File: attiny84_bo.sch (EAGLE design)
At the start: 9 parts, among them J1 AVR_SPI_PRG_6NS, Y1 16MHz

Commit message: initial placement
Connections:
- new net N$6: JP1.10, U$1.(PCINT10/INT0/OC0A/CKOUT)PB2
- net +5V: now also JP1.2, LED1.A
- net GND: now also JP1.16, JP1.4, JP1.6, JP1.8
- net N$1: now also LED1.C
- net PB0/XTAL1: now also JP1.14
- net PB1/XTAL2: now also JP1.12
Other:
- moved on the sheet: LED1
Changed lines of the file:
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@@
 <part name="P+1" library="supply1" deviceset="+5V" device=""/>
 <part name="JP1" library="pinhead" deviceset="PINHD-2X8" device=""/>
+<part name="GND1" library="supply1" deviceset="GND" device=""/>
+<part name="P+2" library="supply1" deviceset="+5V" device=""/>
+<part name="GND2" library="supply1" deviceset="GND" device=""/>
 </parts>
 <sheets>
@@
 <instance part="P+5" gate="1" x="76.2" y="111.76"/>
 <instance part="C1" gate="G$1" x="38.1" y="96.52" rot="R90"/>
-<instance part="LED1" gate="G$1" x="55.88" y="124.46" rot="R270"/>
+<instance part="LED1" gate="G$1" x="109.22" y="91.44" rot="R270"/>
 <instance part="C2" gate="G$1" x="38.1" y="106.68" rot="R90"/>
 <instance part="CX0" gate="G$1" x="20.32" y="104.14" rot="R90"/>
@@
 <instance part="P+1" gate="1" x="20.32" y="86.36"/>
 <instance part="JP1" gate="A" x="121.92" y="63.5"/>
+<instance part="GND1" gate="1" x="127" y="50.8"/>
+<instance part="P+2" gate="1" x="127" y="73.66"/>
+<instance part="GND2" gate="1" x="129.54" y="68.58" rot="R90"/>
 </instances>
 <busses>
@@
 <pinref part="GND3" gate="1" pin="GND"/>
 </segment>
+<segment>
+<pinref part="JP1" gate="A" pin="16"/>
+<pinref part="GND1" gate="1" pin="GND"/>
+</segment>
+<segment>
+<pinref part="JP1" gate="A" pin="4"/>
+<pinref part="GND2" gate="1" pin="GND"/>
+<pinref part="JP1" gate="A" pin="8"/>
+<wire x1="127" y1="68.58" x2="127" y2="66.04" width="0.1524" layer="91"/>
+<junction x="127" y="68.58"/>
+<pinref part="JP1" gate="A" pin="6"/>
+<junction x="127" y="66.04"/>
+<wire x1="127" y1="66.04" x2="127" y2="63.5" width="0.1524" layer="91"/>
+<junction x="127" y="63.5"/>
+</segment>
 </net>
 <net name="+5V" class="1">
@@
 <wire x1="78.74" y1="119.38" x2="35.56" y2="119.38" width="0.1524" layer="91"/>
 <wire x1="35.56" y1="119.38" x2="35.56" y2="106.68" width="0.1524" layer="91"/>
+<pinref part="LED1" gate="G$1" pin="A"/>
+<wire x1="78.74" y1="109.22" x2="111.76" y2="109.22" width="0.1524" layer="91"/>
+<wire x1="111.76" y1="109.22" x2="111.76" y2="91.44" width="0.1524" layer="91"/>
 </segment>
 <segment>
 <pinref part="U$1" gate="G$1" pin="VCC"/>
 <pinref part="P+1" gate="1" pin="+5V"/>
+</segment>
+<segment>
+<pinref part="JP1" gate="A" pin="2"/>
+<pinref part="P+2" gate="1" pin="+5V"/>
 </segment>
 </net>
@@
 <wire x1="10.16" y1="43.18" x2="10.16" y2="91.44" width="0.1524" layer="91"/>
 <wire x1="25.4" y1="91.44" x2="10.16" y2="91.44" width="0.1524" layer="91"/>
+<wire x1="78.74" y1="76.2" x2="137.16" y2="76.2" width="0.1524" layer="91"/>
+<wire x1="137.16" y1="76.2" x2="137.16" y2="55.88" width="0.1524" layer="91"/>
+<pinref part="JP1" gate="A" pin="14"/>
+<wire x1="137.16" y1="55.88" x2="127" y2="55.88" width="0.1524" layer="91"/>
+<junction x="78.74" y="76.2"/>
 </segment>
 </net>
@@
 <wire x1="76.2" y1="78.74" x2="71.12" y2="78.74" width="0.1524" layer="91"/>
 <junction x="25.4" y="104.14"/>
+<wire x1="76.2" y1="78.74" x2="139.7" y2="78.74" width="0.1524" layer="91"/>
+<wire x1="139.7" y1="78.74" x2="139.7" y2="58.42" width="0.1524" layer="91"/>
+<pinref part="JP1" gate="A" pin="12"/>
+<wire x1="127" y1="58.42" x2="139.7" y2="58.42" width="0.1524" layer="91"/>
 </segment>
 </net>
@@
 <pinref part="JP1" gate="A" pin="15"/>
 <wire x1="96.52" y1="53.34" x2="119.38" y2="53.34" width="0.1524" layer="91"/>
+<wire x1="96.52" y1="71.12" x2="96.52" y2="91.44" width="0.1524" layer="91"/>
+<pinref part="LED1" gate="G$1" pin="C"/>
+<wire x1="96.52" y1="91.44" x2="104.14" y2="91.44" width="0.1524" layer="91"/>
+<junction x="96.52" y="71.12"/>
 </segment>
 </net>
@@
 </segment>
 </net>
+<net name="N$6" class="0">
+<segment>
+<pinref part="U$1" gate="G$1" pin="(PCINT10/INT0/OC0A/CKOUT)PB2"/>
+<wire x1="71.12" y1="81.28" x2="134.62" y2="81.28" width="0.1524" layer="91"/>
+<wire x1="134.62" y1="81.28" x2="134.62" y2="60.96" width="0.1524" layer="91"/>
+<pinref part="JP1" gate="A" pin="10"/>
+<wire x1="134.62" y1="60.96" x2="127" y2="60.96" width="0.1524" layer="91"/>
+</segment>
+</net>

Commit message: routed
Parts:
- added H1, H2: MOUNT-PAD-ROUND3.0, holes:MOUNT-PAD-ROUND3.0
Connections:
- net GND: now also H1.MOUNT, H2.MOUNT
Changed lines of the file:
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@@
 <part name="P+2" library="supply1" deviceset="+5V" device=""/>
 <part name="GND2" library="supply1" deviceset="GND" device=""/>
+<part name="H1" library="holes" deviceset="MOUNT-PAD-ROUND" device="3.0"/>
+<part name="GND6" library="supply1" deviceset="GND" device=""/>
+<part name="H2" library="holes" deviceset="MOUNT-PAD-ROUND" device="3.0"/>
+<part name="GND7" library="supply1" deviceset="GND" device=""/>
 </parts>
 <sheets>
@@
 <instance part="P+2" gate="1" x="127" y="73.66"/>
 <instance part="GND2" gate="1" x="129.54" y="68.58" rot="R90"/>
+<instance part="H1" gate="G$1" x="99.06" y="127" rot="R90"/>
+<instance part="GND6" gate="1" x="99.06" y="121.92"/>
+<instance part="H2" gate="G$1" x="111.76" y="127" rot="R90"/>
+<instance part="GND7" gate="1" x="111.76" y="121.92"/>
 </instances>
 <busses>
@@
 <junction x="127" y="63.5"/>
 </segment>
+<segment>
+<pinref part="H1" gate="G$1" pin="MOUNT"/>
+<pinref part="GND6" gate="1" pin="GND"/>
+</segment>
+<segment>
+<pinref part="H2" gate="G$1" pin="MOUNT"/>
+<pinref part="GND7" gate="1" pin="GND"/>
+</segment>
 </net>

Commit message: signal names
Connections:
- net N$1 renamed PA7
- net N$2 renamed PA3
- net N$3 renamed PA2
- net N$4 renamed PA1
- net N$5 renamed PA0
- net N$6 renamed PB2
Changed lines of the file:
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@@
 </segment>
 </net>
-<net name="N$1" class="0">
+<net name="PA7" class="0">
 <segment>
 <pinref part="U$1" gate="G$1" pin="(PCINT7/ICP/OC0B/ADC7)PA7"/>
@@
 </segment>
 </net>
-<net name="N$2" class="0">
+<net name="PA3" class="0">
 <segment>
 <pinref part="U$1" gate="G$1" pin="(PCINT3/T0/ADC3)PA3"/>
@@
 </segment>
 </net>
-<net name="N$3" class="0">
+<net name="PA2" class="0">
 <segment>
 <pinref part="U$1" gate="G$1" pin="(PCINT2/AIN1/ADC2)PA2"/>
@@
 </segment>
 </net>
-<net name="N$4" class="0">
+<net name="PA1" class="0">
 <segment>
 <pinref part="U$1" gate="G$1" pin="(PCINT1/AIN0/ADC1)PA1"/>
@@
 </segment>
 </net>
-<net name="N$5" class="0">
+<net name="PA0" class="0">
 <segment>
 <pinref part="U$1" gate="G$1" pin="(PCINT0/AREF/ADC0)PA0"/>
@@
 </segment>
 </net>
-<net name="N$6" class="0">
+<net name="PB2" class="0">
 <segment>
 <pinref part="U$1" gate="G$1" pin="(PCINT10/INT0/OC0A/CKOUT)PB2"/>

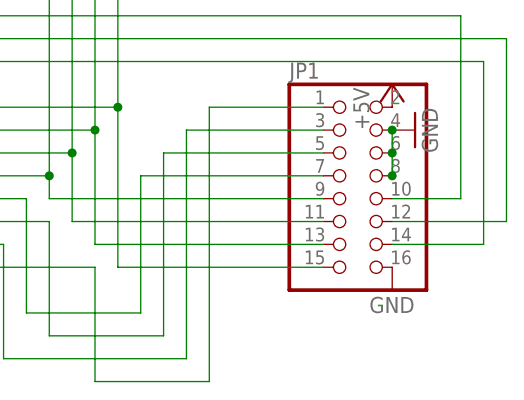
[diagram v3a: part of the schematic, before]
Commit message: second 5v input
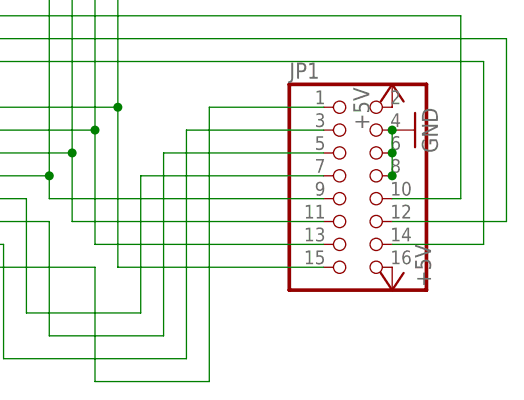
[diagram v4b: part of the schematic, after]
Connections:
- net +5V: now also JP1.16
- net GND: no longer JP1.16
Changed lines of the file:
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@@
 <part name="P+1" library="supply1" deviceset="+5V" device=""/>
 <part name="JP1" library="pinhead" deviceset="PINHD-2X8" device=""/>
-<part name="GND1" library="supply1" deviceset="GND" device=""/>
 <part name="P+2" library="supply1" deviceset="+5V" device=""/>
 <part name="GND2" library="supply1" deviceset="GND" device=""/>
@@
 <part name="H2" library="holes" deviceset="MOUNT-PAD-ROUND" device="3.0"/>
 <part name="GND7" library="supply1" deviceset="GND" device=""/>
+<part name="P+3" library="supply1" deviceset="+5V" device=""/>
 </parts>
 <sheets>
@@
 <instance part="P+1" gate="1" x="20.32" y="86.36"/>
 <instance part="JP1" gate="A" x="121.92" y="63.5"/>
-<instance part="GND1" gate="1" x="127" y="50.8"/>
 <instance part="P+2" gate="1" x="127" y="73.66"/>
 <instance part="GND2" gate="1" x="129.54" y="68.58" rot="R90"/>
@@
 <instance part="H2" gate="G$1" x="111.76" y="127" rot="R90"/>
 <instance part="GND7" gate="1" x="111.76" y="121.92"/>
+<instance part="P+3" gate="1" x="127" y="50.8" rot="R180"/>
 </instances>
 <busses>
@@
 <pinref part="U$1" gate="G$1" pin="GND"/>
 <pinref part="GND3" gate="1" pin="GND"/>
-</segment>
-<segment>
-<pinref part="JP1" gate="A" pin="16"/>
-<pinref part="GND1" gate="1" pin="GND"/>
 </segment>
 <segment>
@@
 <pinref part="P+2" gate="1" pin="+5V"/>
 </segment>
+<segment>
+<pinref part="JP1" gate="A" pin="16"/>
+<pinref part="P+3" gate="1" pin="+5V"/>
+</segment>
 </net>
